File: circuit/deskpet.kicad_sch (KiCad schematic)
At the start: 2 parts, among them J2 AHT20

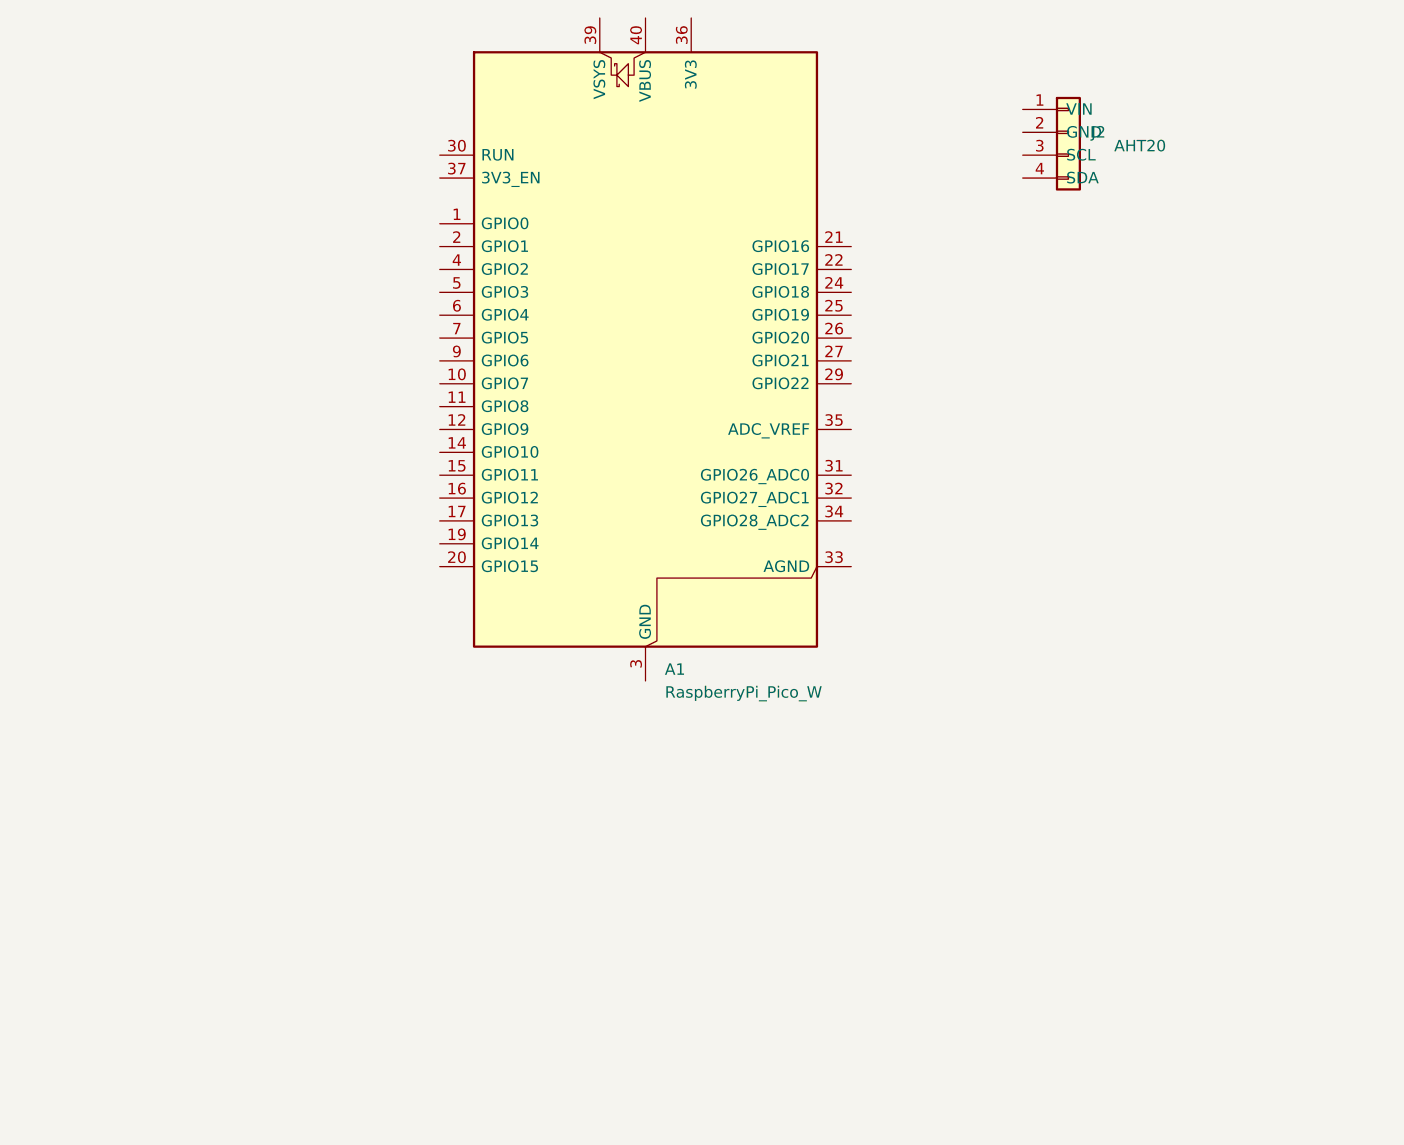
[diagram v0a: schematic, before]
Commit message: added all the boards incl amp speaker temp sensor and screen, and wired them all...
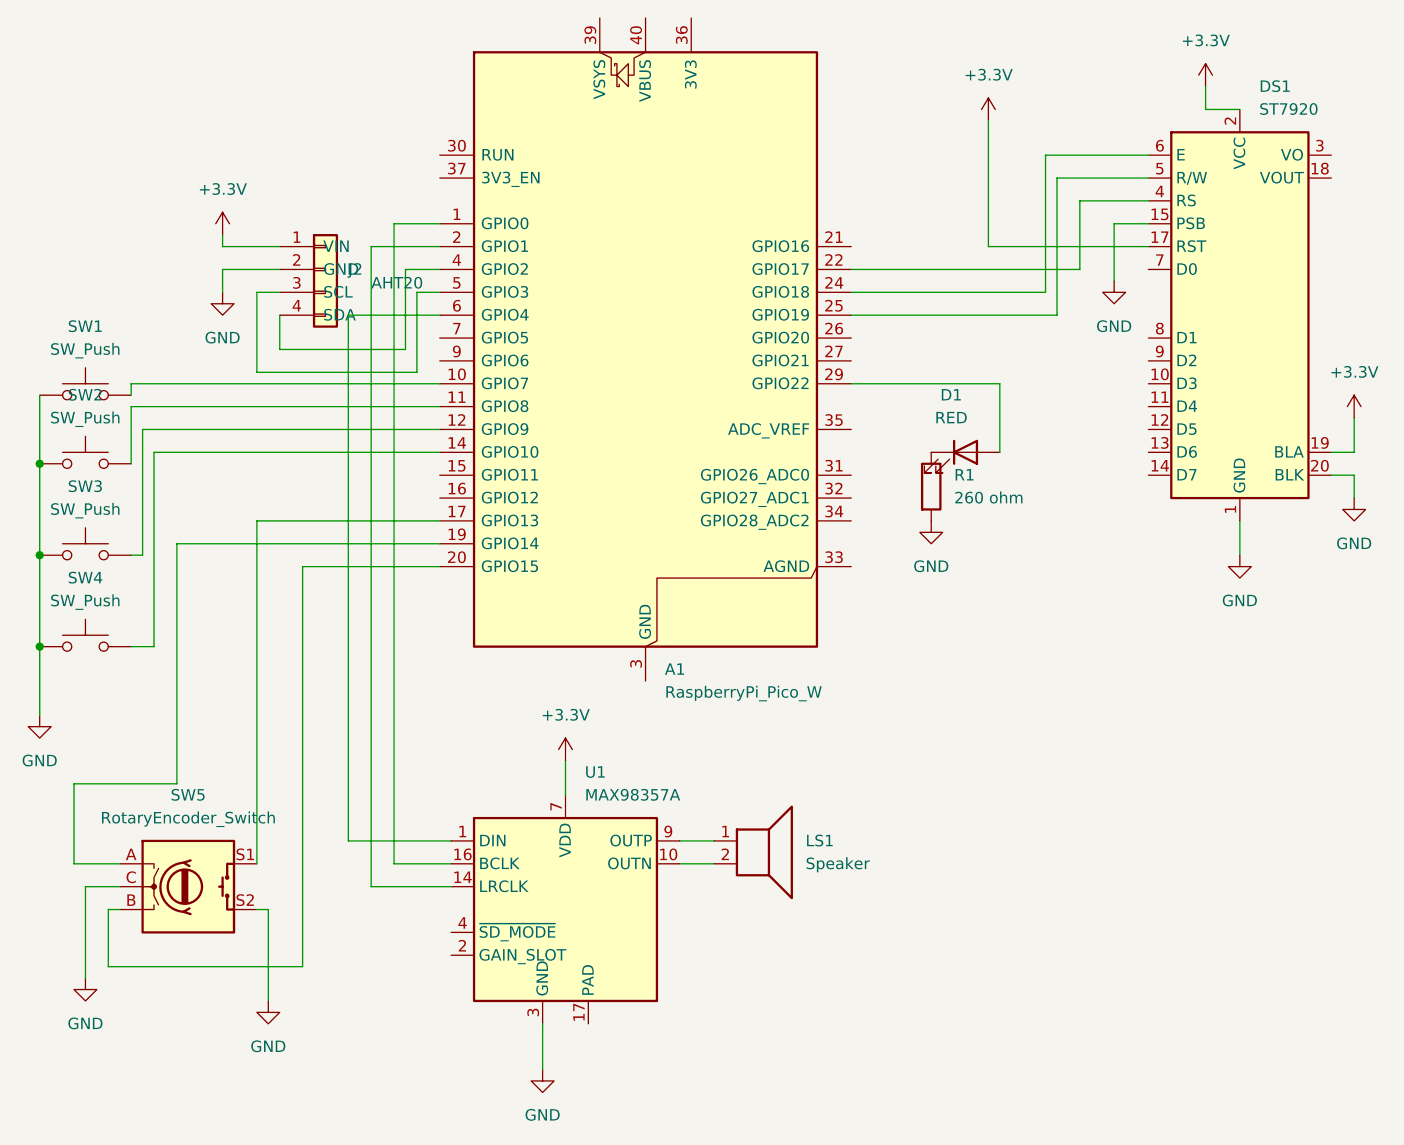
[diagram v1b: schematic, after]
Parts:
- added D1: RED, symbol Device:LED
- added DS1: ST7920, Display:ST7920_128x64, symbol Display_Graphic:ST7920
- added LS1: Speaker, symbol Device:Speaker
- added R1: 260 ohm, symbol Device:R
- added SW1, SW2, SW3, SW4: SW_Push, symbol Switch:SW_Push
- added SW5: RotaryEncoder_Switch, symbol Device:RotaryEncoder_Switch
- added U1: MAX98357A, Package_DFN_QFN:TQFN-16-1EP_3x3mm_P0.5mm_EP1.23x1.23mm, symbol Audio:MAX98357A
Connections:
- net +3.3V: now reaches J2.1 (VIN)
- net +3.3V: now also DS1.17 (RST), DS1.19 (BLA), DS1.2 (VCC), U1.7 (VDD), U1.8 (VDD)
- net GND: now reaches J2.2 (GND)
- net GND: now also DS1.1 (GND), DS1.15 (PSB), DS1.20 (BLK), R1.2, SW1.1, SW2.1, SW3.1, SW4.1, SW5.C, SW5.S2, U1.11 (GND), U1.15 (GND), U1.3 (GND)
- net at J2.3 (SCL): now also A1.5 (GPIO3)
- net at J2.4 (SDA): now also A1.4 (GPIO2)
- net at A1.1 (GPIO0): now also U1.16 (BCLK)
- net at A1.10 (GPIO7): now also SW1.2
- net at A1.11 (GPIO8): now also SW2.2
- net at A1.12 (GPIO9): now also SW3.2
- net at A1.14 (GPIO10): now also SW4.2
- net at A1.17 (GPIO13): now also SW5.S1
- net at A1.19 (GPIO14): now also SW5.A
- net at A1.2 (GPIO1): now also U1.14 (LRCLK)
- net at A1.20 (GPIO15): now also SW5.B
- net at A1.22 (GPIO17): now also DS1.4 (RS)
- net at A1.24 (GPIO18): now also DS1.6 (E)
- net at A1.25 (GPIO19): now also DS1.5 (R/W)
- net at A1.29 (GPIO22): now also D1.2 (A)
- net at A1.6 (GPIO4): now also U1.1 (DIN)
- new net: D1.1 (K), R1.1
- new net: LS1.1, U1.9 (OUTP)
- new net: LS1.2, U1.10 (OUTN)
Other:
- moved on the sheet: J2
